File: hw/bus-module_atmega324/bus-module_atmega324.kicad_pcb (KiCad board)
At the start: 2 copper layers, 35 x 48 mm, 36 parts, among them J1 CONN_10X2, J2 CONN_10X2, J3 CONN-ISP-6, J5 CONN_1, J6 CONN_1, J7 CONN_1, J8 CONN_1, U1 ATMEGA324-TQFP44, U2 7,3728MHz, U3 25LCXXX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

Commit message: R2, R3, R4 100 Ohms
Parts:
- R2, R3, R4: value 1k -> 100
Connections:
- D2 pad 2: (no net) -> Net-(D2-Pad2)
- H1 pad 1: (no net) -> Net-(H1-Pad1)
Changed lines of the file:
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@@
-(kicad_pcb (version 20171130) (host pcbnew 5.0.0-fee4fd1~66~ubuntu16.04.1)
+(kicad_pcb (version 20171130) (host pcbnew 5.0.2-bee76a0~70~ubuntu18.04.1)
   (general
     (thickness 1.6)
@@
     (zones 0)
     (modules 36)
-    (nets 52)
+    (nets 54)
   )
   (page A4)
@@
     (pad_drill 2.5)
     (pad_to_mask_clearance 0)
+    (solder_mask_min_width 0.25)
     (aux_axis_origin 0 0)
     (grid_origin 88.57 83.3875)
@@
   (net 50 "Net-(F1-Pad1)")
   (net 51 VCC)
+  (net 52 "Net-(D2-Pad2)")
+  (net 53 "Net-(H1-Pad1)")
   (net_class Default "This is the default net class."
     (clearance 0.2)
@@
     (add_net "Net-(C1-Pad2)")
     (add_net "Net-(C2-Pad2)")
+    (add_net "Net-(D2-Pad2)")
     (add_net "Net-(F1-Pad1)")
+    (add_net "Net-(H1-Pad1)")
     (add_net "Net-(R1-Pad2)")
     (add_net "Net-(R5-Pad2)")
@@
     (add_net +24V)
     (add_net GND)
-    (add_net "Net-(F1-Pad2)")
   )
   (module Connector_Header:HEADER_3x2 (layer B.Cu)
@@
     (pad 3 smd rect (at 0.95 -0.95 90) (size 0.85 0.85) (layers F.Cu F.Paste F.Mask)
       (net 49 /B))
-    (pad 2 smd rect (at 0.95 0.95 90) (size 0.85 0.85) (layers F.Cu F.Paste F.Mask))
+    (pad 2 smd rect (at 0.95 0.95 90) (size 0.85 0.85) (layers F.Cu F.Paste F.Mask)
+      (net 52 "Net-(D2-Pad2)"))
     (pad 1 smd rect (at -0.76962 0.95 90) (size 1.2 0.85) (layers F.Cu F.Paste F.Mask)
       (net 1 GND))
@@
       (effects (font (size 0.8 0.8) (thickness 0.15)))
     )
-    (fp_text value 1k (at 0.127 1.524 45) (layer F.Fab)
+    (fp_text value 100 (at 0.127 1.524 45) (layer F.Fab)
       (effects (font (size 0.8 0.8) (thickness 0.15)))
     )
@@
       (effects (font (size 0.8 0.8) (thickness 0.15)))
     )
-    (fp_text value 1k (at 0.127 1.524 45) (layer F.Fab)
+    (fp_text value 100 (at 0.127 1.524 45) (layer F.Fab)
       (effects (font (size 0.8 0.8) (thickness 0.15)))
     )
@@
       (effects (font (size 0.8 0.8) (thickness 0.15)))
     )
-    (fp_text value 1k (at 0.127 1.524 45) (layer F.Fab)
+    (fp_text value 100 (at 0.127 1.524 45) (layer F.Fab)
       (effects (font (size 0.8 0.8) (thickness 0.15)))
     )
@@
     (fp_line (start -2.54 2.54) (end 2.54 2.54) (layer F.SilkS) (width 0.254))
     (fp_line (start 2.54 2.54) (end 2.54 -2.54) (layer F.SilkS) (width 0.254))
-    (pad 1 thru_hole circle (at 0 0) (size 3.5 3.5) (drill 2.5) (layers *.Cu *.Mask F.SilkS))
+    (pad 1 thru_hole circle (at 0 0) (size 3.5 3.5) (drill 2.5) (layers *.Cu *.Mask F.SilkS)
+      (net 53 "Net-(H1-Pad1)"))
   )
   (module Housings_QFP:TQFP-44_10x10mm_Pitch0.8mm (layer F.Cu)
@@
   (segment (start 102.409603 95.577372) (end 103.019128 94.967847) (width 0.3) (layer F.Cu) (net 3))
   (segment (start 102.409603 95.577372) (end 102.422628 95.577372) (width 0.3) (layer F.Cu) (net 3) (status 30))
-  (segment (start 100.863852 112.928274) (end 101.263851 113.328273) (width 0.6) (layer F.Cu) (net 51))
-  (segment (start 100.762 112.826422) (end 100.863852 112.928274) (width 0.6) (layer F.Cu) (net 51))
-  (segment (start 100.762 109.8035) (end 100.762 112.826422) (width 0.6) (layer F.Cu) (net 51))
-  (segment (start 101.232624 113.3595) (end 101.263851 113.328273) (width 0.6) (layer B.Cu) (net 51))
-  (segment (start 88.062 113.3595) (end 101.232624 113.3595) (width 0.6) (layer B.Cu) (net 51))
-  (via (at 101.263851 113.328273) (size 0.8) (drill 0.4) (layers F.Cu B.Cu) (net 51))
-  (segment (start 109.144 112.3435) (end 108.128 112.3435) (width 0.6) (layer B.Cu) (net 51))
-  (via (at 109.144 112.3435) (size 0.8) (drill 0.4) (layers F.Cu B.Cu) (net 51))
-  (segment (start 109.56564 111.3275) (end 109.144 111.3275) (width 0.6) (layer B.Cu) (net 51))
-  (segment (start 109.144 111.3275) (end 108.128 112.3435) (width 0.6) (layer B.Cu) (net 51))
-  (via (at 108.128 112.3435) (size 0.8) (drill 0.4) (layers F.Cu B.Cu) (net 51))
-  (via (at 88.062 113.3595) (size 0.8) (drill 0.4) (layers F.Cu B.Cu) (net 51))
-  (segment (start 100.3175 95.948525) (end 100.3175 96.409113) (width 0.6) (layer B.Cu) (net 51))
-  (segment (start 100.3175 96.409113) (end 99.043497 96.409113) (width 0.6) (layer B.Cu) (net 51))
-  (segment (start 99.043497 96.409113) (end 98.477812 96.409113) (width 0.6) (layer B.Cu) (net 51))
-  (via (at 98.477812 96.409113) (size 0.8) (drill 0.4) (layers F.Cu B.Cu) (net 51))
-  (segment (start 103.004371 105.356871) (end 103.187619 105.356871) (width 0.3) (layer F.Cu) (net 51))
-  (segment (start 103.296619 105.430517) (end 103.721405 105.855303) (width 0.3) (layer F.Cu) (net 51))
-  (segment (start 103.187619 105.356871) (end 103.261265 105.430517) (width 0.3) (layer F.Cu) (net 51))
-  (segment (start 103.261265 105.430517) (end 103.296619 105.430517) (width 0.3) (layer F.Cu) (net 51))
-  (segment (start 103.721405 105.855303) (end 103.898183 105.855303) (width 0.3) (layer F.Cu) (net 51))
-  (segment (start 103.898183 105.855303) (end 103.924439 105.881559) (width 0.3) (layer F.Cu) (net 51))
-  (segment (start 103.924439 105.881559) (end 104.4475 105.881559) (width 0.3) (layer F.Cu) (net 51))
-  (segment (start 104.4475 105.881559) (end 104.4475 106.8) (width 0.3) (layer F.Cu) (net 51))
-  (segment (start 100.3175 94.8175) (end 100.3175 95.948525) (width 0.6) (layer B.Cu) (net 51))
-  (segment (start 100.3175 95.948525) (end 100.3175 97.3295) (width 0.6) (layer B.Cu) (net 51))
-  (segment (start 100.3175 97.3295) (end 100.333 97.345) (width 0.6) (layer B.Cu) (net 51))
-  (segment (start 91.5 100.9525) (end 91.5 101.75) (width 0.6) (layer B.Cu) (net 51) (status 10))
-  (via (at 91.5 101.75) (size 0.8) (drill 0.4) (layers F.Cu B.Cu) (net 51))
-  (segment (start 91.5 101.75) (end 92.245 102.495) (width 0.6) (layer B.Cu) (net 51) (status 20))
-  (segment (start 91.5 100.9525) (end 91.75 100.7025) (width 0.6) (layer B.Cu) (net 51) (status 30))
-  (segment (start 92.533 102.495) (end 92.245 102.495) (width 0.6) (layer B.Cu) (net 51) (status 30))
   (segment (start 90.475 108.7875) (end 89.586 107.8985) (width 0.3) (layer F.Cu) (net 4))
   (segment (start 89.586 106.819) (end 90.1575 106.2475) (width 0.3) (layer F.Cu) (net 4))
@@
   (segment (start 91.618 107.7715) (end 87.935 104.0885) (width 0.6) (layer B.Cu) (net 50))
   (segment (start 83.1344 101.8279) (end 83.109 101.8279) (width 0.6) (layer F.Cu) (net 50))
+  (segment (start 100.863852 112.928274) (end 101.263851 113.328273) (width 0.6) (layer F.Cu) (net 51))
+  (segment (start 100.762 112.826422) (end 100.863852 112.928274) (width 0.6) (layer F.Cu) (net 51))
+  (segment (start 100.762 109.8035) (end 100.762 112.826422) (width 0.6) (layer F.Cu) (net 51))
+  (segment (start 101.232624 113.3595) (end 101.263851 113.328273) (width 0.6) (layer B.Cu) (net 51))
+  (segment (start 88.062 113.3595) (end 101.232624 113.3595) (width 0.6) (layer B.Cu) (net 51))
+  (via (at 101.263851 113.328273) (size 0.8) (drill 0.4) (layers F.Cu B.Cu) (net 51))
+  (segment (start 109.144 112.3435) (end 108.128 112.3435) (width 0.6) (layer B.Cu) (net 51))
+  (via (at 109.144 112.3435) (size 0.8) (drill 0.4) (layers F.Cu B.Cu) (net 51))
+  (segment (start 109.56564 111.3275) (end 109.144 111.3275) (width 0.6) (layer B.Cu) (net 51))
+  (segment (start 109.144 111.3275) (end 108.128 112.3435) (width 0.6) (layer B.Cu) (net 51))
+  (via (at 108.128 112.3435) (size 0.8) (drill 0.4) (layers F.Cu B.Cu) (net 51))
+  (via (at 88.062 113.3595) (size 0.8) (drill 0.4) (layers F.Cu B.Cu) (net 51))
+  (segment (start 100.3175 95.948525) (end 100.3175 96.409113) (width 0.6) (layer B.Cu) (net 51))
+  (segment (start 100.3175 96.409113) (end 99.043497 96.409113) (width 0.6) (layer B.Cu) (net 51))
+  (segment (start 99.043497 96.409113) (end 98.477812 96.409113) (width 0.6) (layer B.Cu) (net 51))
+  (via (at 98.477812 96.409113) (size 0.8) (drill 0.4) (layers F.Cu B.Cu) (net 51))
+  (segment (start 103.004371 105.356871) (end 103.187619 105.356871) (width 0.3) (layer F.Cu) (net 51))
+  (segment (start 103.296619 105.430517) (end 103.721405 105.855303) (width 0.3) (layer F.Cu) (net 51))
+  (segment (start 103.187619 105.356871) (end 103.261265 105.430517) (width 0.3) (layer F.Cu) (net 51))
+  (segment (start 103.261265 105.430517) (end 103.296619 105.430517) (width 0.3) (layer F.Cu) (net 51))
+  (segment (start 103.721405 105.855303) (end 103.898183 105.855303) (width 0.3) (layer F.Cu) (net 51))
+  (segment (start 103.898183 105.855303) (end 103.924439 105.881559) (width 0.3) (layer F.Cu) (net 51))
+  (segment (start 103.924439 105.881559) (end 104.4475 105.881559) (width 0.3) (layer F.Cu) (net 51))
+  (segment (start 104.4475 105.881559) (end 104.4475 106.8) (width 0.3) (layer F.Cu) (net 51))
+  (segment (start 100.3175 94.8175) (end 100.3175 95.948525) (width 0.6) (layer B.Cu) (net 51))
+  (segment (start 100.3175 95.948525) (end 100.3175 97.3295) (width 0.6) (layer B.Cu) (net 51))
+  (segment (start 100.3175 97.3295) (end 100.333 97.345) (width 0.6) (layer B.Cu) (net 51))
+  (segment (start 91.5 100.9525) (end 91.5 101.75) (width 0.6) (layer B.Cu) (net 51) (status 10))
+  (via (at 91.5 101.75) (size 0.8) (drill 0.4) (layers F.Cu B.Cu) (net 51))
+  (segment (start 91.5 101.75) (end 92.245 102.495) (width 0.6) (layer B.Cu) (net 51) (status 20))
+  (segment (start 91.5 100.9525) (end 91.75 100.7025) (width 0.6) (layer B.Cu) (net 51) (status 30))
+  (segment (start 92.533 102.495) (end 92.245 102.495) (width 0.6) (layer B.Cu) (net 51) (status 30))
   (zone (net 1) (net_name GND) (layer B.Cu) (hatch edge 0.508)
     (connect_pads (clearance 0.254))

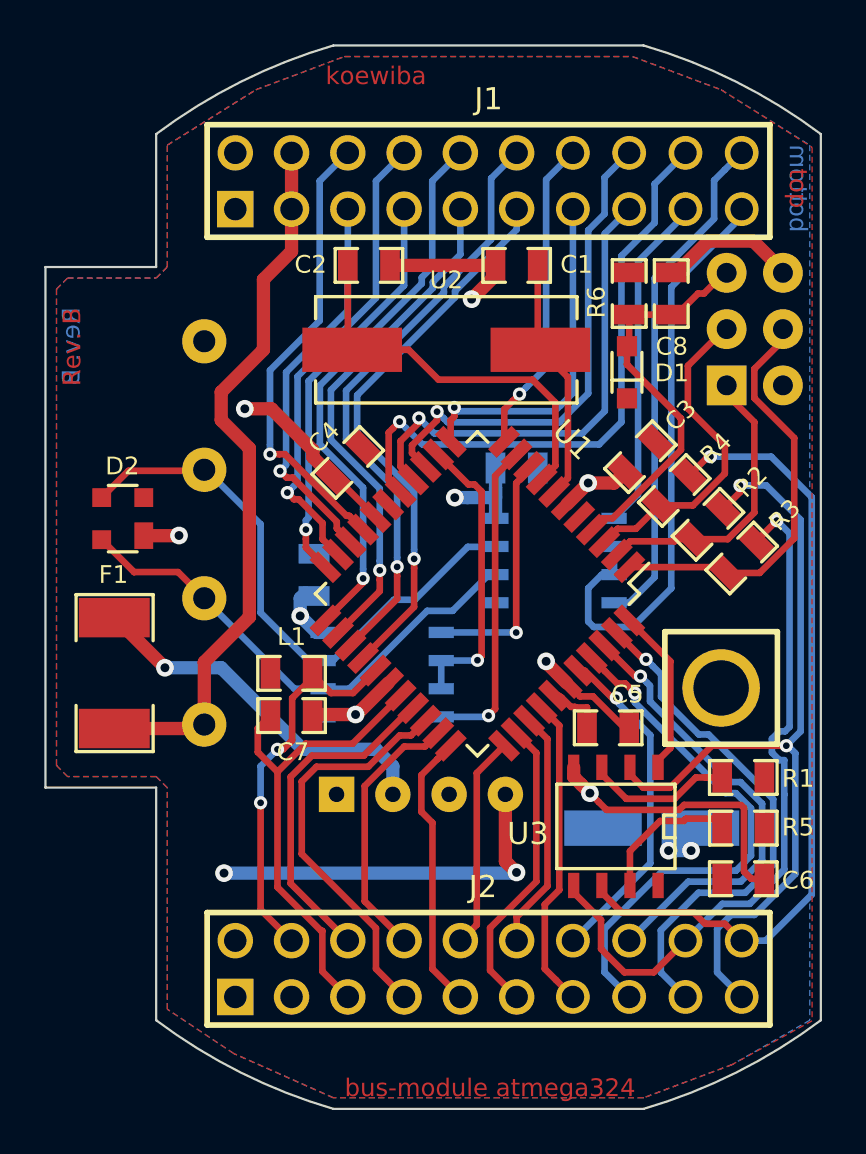
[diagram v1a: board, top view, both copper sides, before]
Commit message: Increase WAGO hole diameter, replace ELKO with keramic capacitor, Increase WAGO hole diameter, update footprints, add pull-down to BUSTXEN, update footprints, set Rev to C
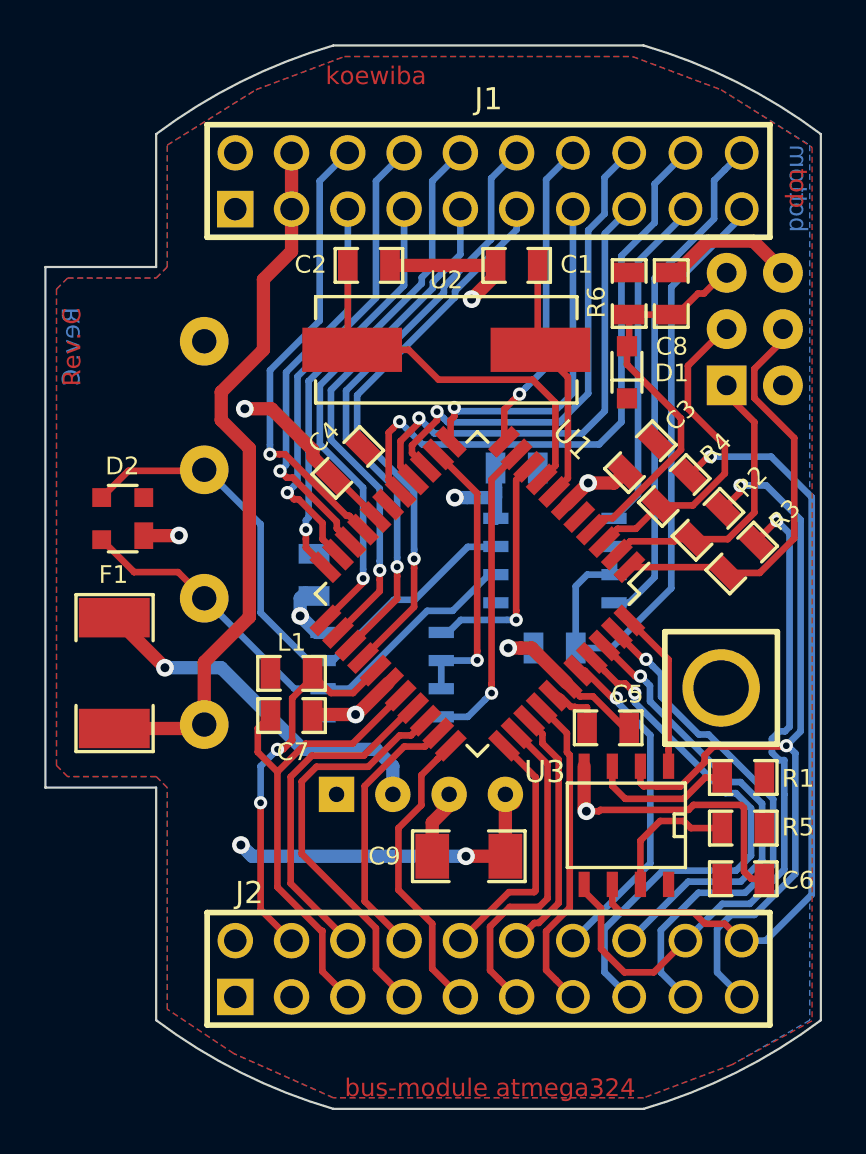
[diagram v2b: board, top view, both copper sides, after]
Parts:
- added R7: 10k, Resistor:R_0805, B.Cu at (103.0, 103.2)
- C9: value 100µF -> 100µF/6,3V VS; footprint Capacitors_SMD:CP_D6.3mm -> Capacitors_SMD:C_1206; moved to F.Cu
- moved C9 8.35 mm to (99.1, 112.6), turned to 180 degrees
- moved U3 0.48 mm to (106.2, 111.2)
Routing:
- net GND: track 48.0 -> 54.0 mm
- net VCC: track 29.7 -> 25.4 mm, vias 6 -> 4
- net /BUSTXDEN: track 27.5 -> 30.2 mm
- net /PA3: track 9.67 -> 12.1 mm
- net /PA2: track 13.6 -> 14.8 mm
- net /PA4: track 12.6 -> 13.5 mm
- net /PA1: track 10.8 -> 11.4 mm
- net /TXD0: track 14.5 -> 14.0 mm
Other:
- board text added: "Rev. C"
- board text removed: "Rev. B"

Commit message: Update to KiCAD6: bus-module_atmega324
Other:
- net class Default removed
- net class Power removed
